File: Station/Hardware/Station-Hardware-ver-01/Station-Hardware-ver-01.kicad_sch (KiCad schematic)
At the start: 28 parts, among them J1 Barrel_Jack, J2 Conn_01x03_Male, J3 Conn_01x03_Male, J4 4P4C, J5 4P4C, J6 Conn_01x03_Male, U1 YAAJ_BluePill, U2 DS3231_Full_Pinout, U3 SX1278_Minimal, U4 MCP6002-xP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

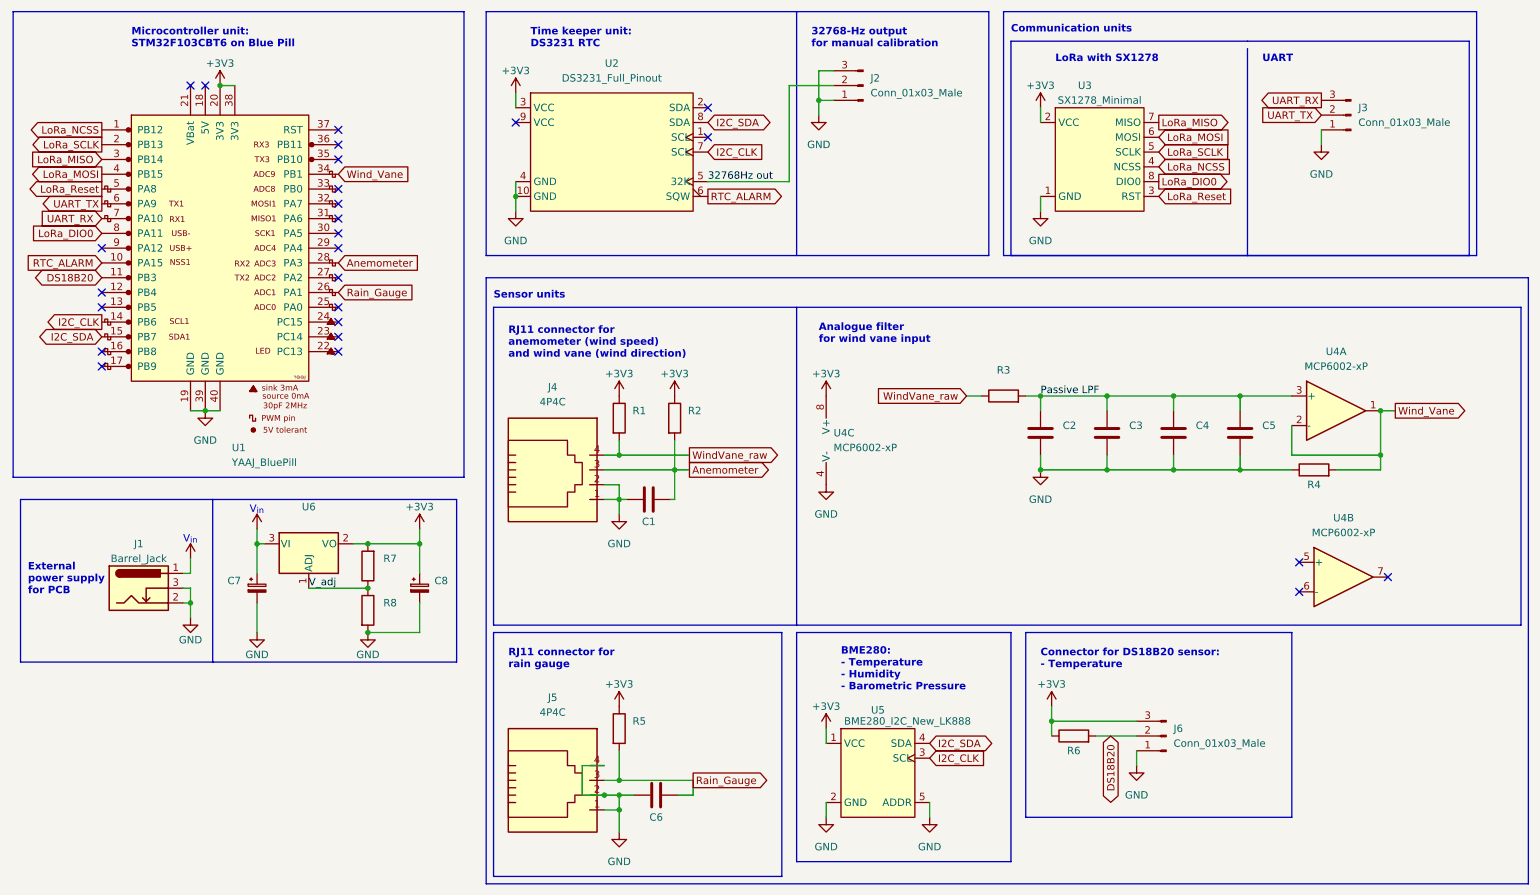
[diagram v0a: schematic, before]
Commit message: station pcb: update resistors from tht to smt
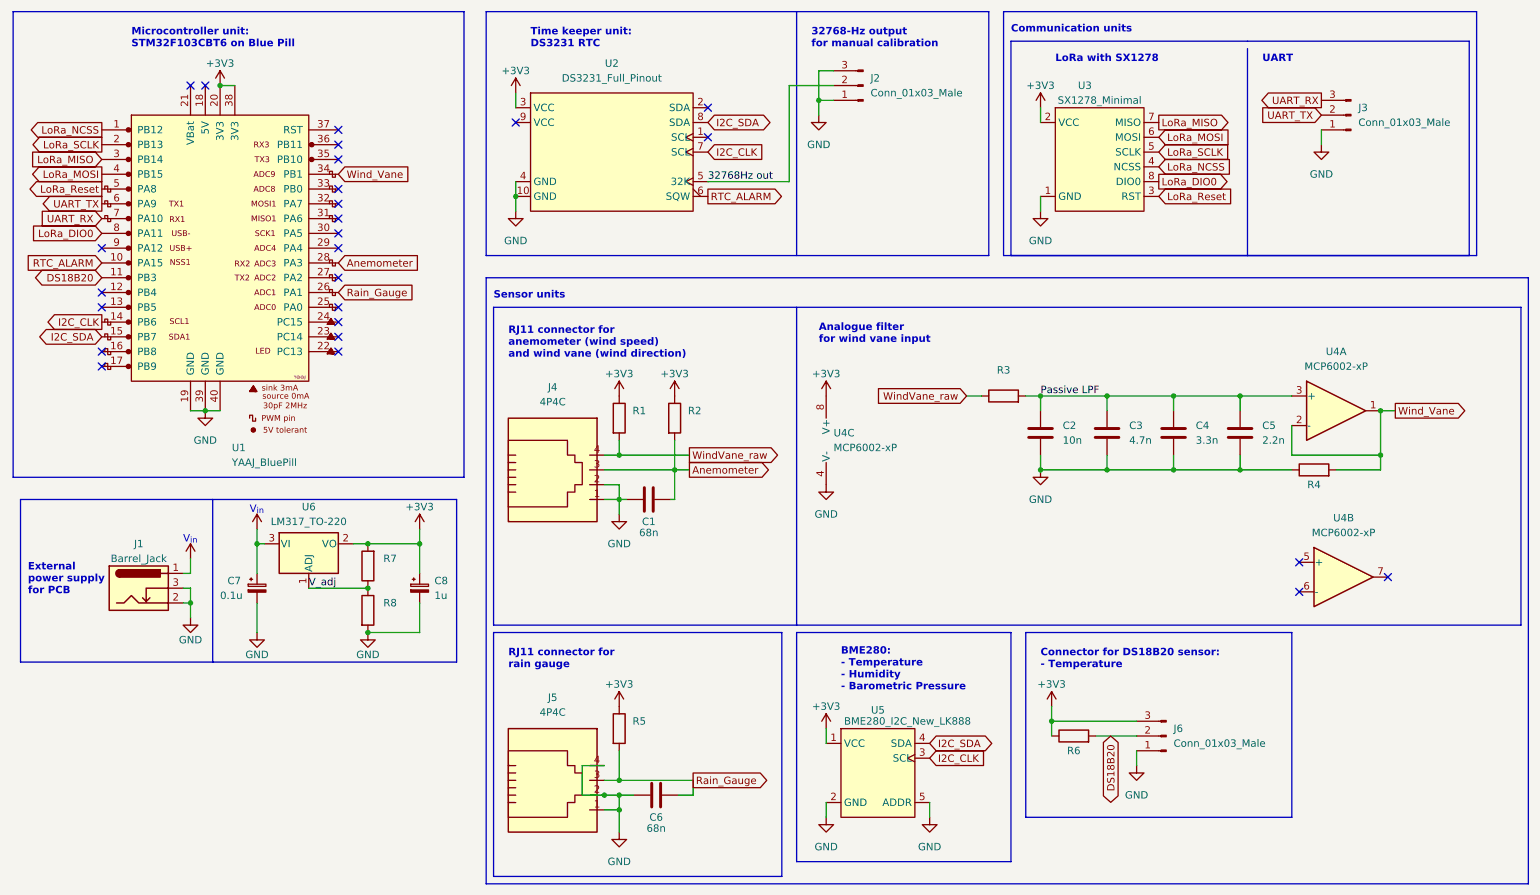
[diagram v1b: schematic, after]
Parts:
- C1, C6: value (none) -> 68n; footprint (none) -> Capacitor_THT:C_Disc_D8.0mm_W5.0mm_P7.50mm
- C2: value (none) -> 10n; footprint (none) -> Capacitor_THT:C_Disc_D5.1mm_W3.2mm_P5.00mm
- C3: value (none) -> 4.7n; footprint (none) -> Capacitor_THT:C_Disc_D5.1mm_W3.2mm_P5.00mm
- C4: value (none) -> 3.3n; footprint (none) -> Capacitor_THT:C_Disc_D5.1mm_W3.2mm_P5.00mm
- C5: value (none) -> 2.2n; footprint (none) -> Capacitor_THT:C_Disc_D5.1mm_W3.2mm_P5.00mm
- C7: value (none) -> 0.1u; footprint (none) -> Capacitor_THT:CP_Radial_D5.0mm_P2.00mm
- C8: value (none) -> 1u; footprint (none) -> Capacitor_THT:CP_Radial_D5.0mm_P2.00mm
- U6: value (none) -> LM317_TO-220; footprint (none) -> Package_TO_SOT_THT:TO-220-3_Vertical
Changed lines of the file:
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@@
     (in_bom yes) (on_board yes)
     (property "Reference" "C1" (id 0) (at 127 101.6 90))
-    (property "Value" "" (id 1) (at 127 103.505 90))
-    (property "Footprint" "" (id 2) (at 130.81 96.8248 0)
+    (property "Value" "68n" (id 1) (at 127 103.505 90))
+    (property "Footprint" "Capacitor_THT:C_Disc_D8.0mm_W5.0mm_P7.50mm" (id 2) (at 130.81 96.8248 0)
       (effects (font (size 1.27 1.27)) hide)
     )
@@
       (effects (font (size 1.27 1.27)) hide)
     )
-    (property "Value" "" (id 1) (at 48.26 102.87 0)
+    (property "Value" "VCC" (id 1) (at 48.26 102.87 0)
       (effects (font (size 1.27 1.27)) hide)
     )
@@
       (effects (font (size 1.27 1.27)) (justify left))
     )
-    (property "Value" "" (id 1) (at 53.34 114.3 0)
-      (effects (font (size 1.27 1.27)) (justify left))
-    )
-    (property "Footprint" "" (id 2) (at 59.69 113.03 0)
+    (property "Value" "0.1u" (id 1) (at 53.34 114.3 0)
+      (effects (font (size 1.27 1.27)) (justify left))
+    )
+    (property "Footprint" "Capacitor_THT:CP_Radial_D5.0mm_P2.00mm" (id 2) (at 59.69 113.03 0)
       (effects (font (size 1.27 1.27)) hide)
     )
@@
       (effects (font (size 1.27 1.27)) (justify left))
     )
-    (property "Value" "" (id 1) (at 90.17 114.3 0)
-      (effects (font (size 1.27 1.27)) (justify left))
-    )
-    (property "Footprint" "" (id 2) (at 87.63 113.03 0)
+    (property "Value" "1u" (id 1) (at 90.17 114.3 0)
+      (effects (font (size 1.27 1.27)) (justify left))
+    )
+    (property "Footprint" "Capacitor_THT:CP_Radial_D5.0mm_P2.00mm" (id 2) (at 87.63 113.03 0)
       (effects (font (size 1.27 1.27)) hide)
     )
@@
       (effects (font (size 1.27 1.27)) (justify left))
     )
-    (property "Value" "" (id 1) (at 198.12 87.6299 0)
-      (effects (font (size 1.27 1.27)) (justify left))
-    )
-    (property "Footprint" "" (id 2) (at 195.2752 90.17 0)
+    (property "Value" "10n" (id 1) (at 198.12 87.6299 0)
+      (effects (font (size 1.27 1.27)) (justify left))
+    )
+    (property "Footprint" "Capacitor_THT:C_Disc_D5.1mm_W3.2mm_P5.00mm" (id 2) (at 195.2752 90.17 0)
       (effects (font (size 1.27 1.27)) hide)
     )
@@
     (in_bom yes) (on_board yes)
     (property "Reference" "U6" (id 0) (at 68.58 99.06 0))
-    (property "Value" "" (id 1) (at 68.58 101.6 0))
-    (property "Footprint" "" (id 2) (at 68.58 99.06 0)
+    (property "Value" "LM317_TO-220" (id 1) (at 68.58 101.6 0))
+    (property "Footprint" "Package_TO_SOT_THT:TO-220-3_Vertical" (id 2) (at 68.58 99.06 0)
       (effects (font (size 1.27 1.27) italic) hide)
     )
@@
       (effects (font (size 1.27 1.27)) (justify left))
     )
-    (property "Value" "" (id 1) (at 209.55 87.6299 0)
-      (effects (font (size 1.27 1.27)) (justify left))
-    )
-    (property "Footprint" "" (id 2) (at 206.7052 90.17 0)
+    (property "Value" "4.7n" (id 1) (at 209.55 87.6299 0)
+      (effects (font (size 1.27 1.27)) (justify left))
+    )
+    (property "Footprint" "Capacitor_THT:C_Disc_D5.1mm_W3.2mm_P5.00mm" (id 2) (at 206.7052 90.17 0)
       (effects (font (size 1.27 1.27)) hide)
     )
@@
       (effects (font (size 1.27 1.27)) (justify left))
     )
-    (property "Value" "" (id 1) (at 232.41 87.6299 0)
-      (effects (font (size 1.27 1.27)) (justify left))
-    )
-    (property "Footprint" "" (id 2) (at 229.5652 90.17 0)
+    (property "Value" "2.2n" (id 1) (at 232.41 87.6299 0)
+      (effects (font (size 1.27 1.27)) (justify left))
+    )
+    (property "Footprint" "Capacitor_THT:C_Disc_D5.1mm_W3.2mm_P5.00mm" (id 2) (at 229.5652 90.17 0)
       (effects (font (size 1.27 1.27)) hide)
     )
@@
     (in_bom yes) (on_board yes)
     (property "Reference" "C6" (id 0) (at 128.27 152.4 90))
-    (property "Value" "" (id 1) (at 128.27 154.305 90))
-    (property "Footprint" "" (id 2) (at 132.08 147.6248 0)
+    (property "Value" "68n" (id 1) (at 128.27 154.305 90))
+    (property "Footprint" "Capacitor_THT:C_Disc_D8.0mm_W5.0mm_P7.50mm" (id 2) (at 132.08 147.6248 0)
       (effects (font (size 1.27 1.27)) hide)
     )
@@
       (effects (font (size 1.27 1.27)) (justify left))
     )
-    (property "Value" "" (id 1) (at 220.98 87.6299 0)
-      (effects (font (size 1.27 1.27)) (justify left))
-    )
-    (property "Footprint" "" (id 2) (at 218.1352 90.17 0)
+    (property "Value" "3.3n" (id 1) (at 220.98 87.6299 0)
+      (effects (font (size 1.27 1.27)) (justify left))
+    )
+    (property "Footprint" "Capacitor_THT:C_Disc_D5.1mm_W3.2mm_P5.00mm" (id 2) (at 218.1352 90.17 0)
       (effects (font (size 1.27 1.27)) hide)
     )
@@
     )
     (path "/b3ed612d-4b95-418f-bfae-ed954c910011"
-      (reference "R1") (unit 1) (value "3k") (footprint "Resistor_THT:R_Axial_DIN0207_L6.3mm_D2.5mm_P10.16mm_Horizontal")
+      (reference "R1") (unit 1) (value "3k") (footprint "Resistor_SMD:R_1206_3216Metric_Pad1.30x1.75mm_HandSolder")
     )
     (path "/e78c6541-571c-4ae3-b37a-ce88f45e4767"
-      (reference "R2") (unit 1) (value "33k") (footprint "Resistor_THT:R_Axial_DIN0207_L6.3mm_D2.5mm_P10.16mm_Horizontal")
+      (reference "R2") (unit 1) (value "33k") (footprint "Resistor_SMD:R_1206_3216Metric_Pad1.30x1.75mm_HandSolder")
     )
     (path "/f24191bb-7c3d-46c7-90d2-d6965006ff76"
-      (reference "R3") (unit 1) (value "680") (footprint "Resistor_THT:R_Axial_DIN0207_L6.3mm_D2.5mm_P10.16mm_Horizontal")
+      (reference "R3") (unit 1) (value "680") (footprint "Resistor_SMD:R_1206_3216Metric_Pad1.30x1.75mm_HandSolder")
     )
     (path "/a225e9fd-6545-4110-8e72-7e9c999e5896"
-      (reference "R4") (unit 1) (value "3.3k") (footprint "Resistor_THT:R_Axial_DIN0207_L6.3mm_D2.5mm_P10.16mm_Horizontal")
+      (reference "R4") (unit 1) (value "3.3k") (footprint "Resistor_SMD:R_1206_3216Metric_Pad1.30x1.75mm_HandSolder")
     )
     (path "/084b112d-dcfd-4801-aa54-60bf427059e5"
-      (reference "R5") (unit 1) (value "33k") (footprint "Resistor_THT:R_Axial_DIN0207_L6.3mm_D2.5mm_P10.16mm_Horizontal")
+      (reference "R5") (unit 1) (value "33k") (footprint "Resistor_SMD:R_1206_3216Metric_Pad1.30x1.75mm_HandSolder")
     )
     (path "/837176e9-8fab-41d2-86dd-da3b1b3dd39f"
-      (reference "R6") (unit 1) (value "4.7k") (footprint "Resistor_THT:R_Axial_DIN0207_L6.3mm_D2.5mm_P10.16mm_Horizontal")
+      (reference "R6") (unit 1) (value "4.7k") (footprint "Resistor_SMD:R_1206_3216Metric_Pad1.30x1.75mm_HandSolder")
     )
     (path "/663da0bb-040e-43a6-982a-c4e18537fdce"
-      (reference "R7") (unit 1) (value "240") (footprint "Resistor_THT:R_Axial_DIN0207_L6.3mm_D2.5mm_P10.16mm_Horizontal")
+      (reference "R7") (unit 1) (value "240") (footprint "Resistor_SMD:R_1206_3216Metric_Pad1.30x1.75mm_HandSolder")
     )
     (path "/8f4c3a00-76f4-4c25-b09e-e3dbef7c09cf"
-      (reference "R8") (unit 1) (value "390") (footprint "Resistor_THT:R_Axial_DIN0207_L6.3mm_D2.5mm_P10.16mm_Horizontal")
+      (reference "R8") (unit 1) (value "390") (footprint "Resistor_SMD:R_1206_3216Metric_Pad1.30x1.75mm_HandSolder")
     )
     (path "/a3f9c6b6-1661-4aed-910d-16d5cf883aed"
